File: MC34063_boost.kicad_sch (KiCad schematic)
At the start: 24 parts, among them U1 MC34063AP

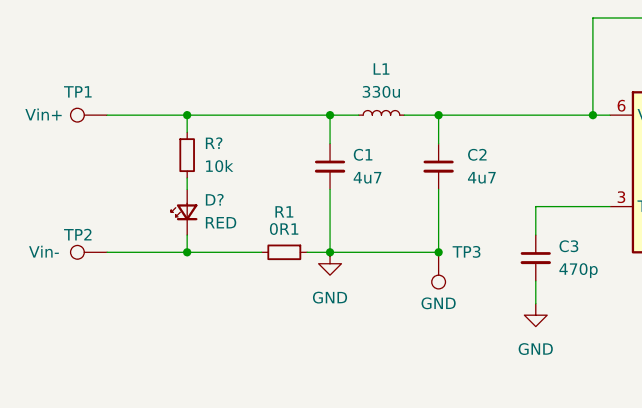
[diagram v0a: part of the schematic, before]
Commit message: Fix: changed LED colour to green
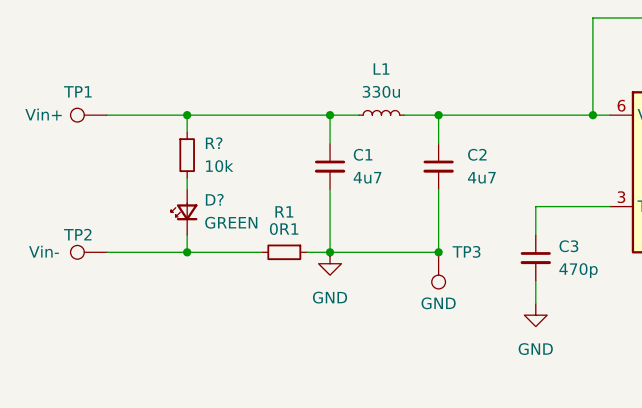
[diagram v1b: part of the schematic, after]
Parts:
- D?: value RED -> GREEN
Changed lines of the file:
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@@
       (effects (font (size 1.27 1.27)) (justify right))
     )
-    (property "Value" "RED" (id 1) (at 86.36 100.9014 90)
+    (property "Value" "GREEN" (id 1) (at 86.36 100.9014 90)
       (effects (font (size 1.27 1.27)) (justify right))
     )
@@
     )
     (path "/f1e8466d-b516-415c-bd57-3e7e0e36268f"
-      (reference "D?") (unit 1) (value "RED") (footprint "")
+      (reference "D?") (unit 1) (value "GREEN") (footprint "")
     )
     (path "/56f0ed1d-b051-4666-80cc-c23759923f3f"
